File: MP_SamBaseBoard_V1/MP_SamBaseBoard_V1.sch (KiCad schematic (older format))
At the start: 135 parts, among them J1 MOTOR-A_CONN, J10 P1_CONN, J11 I2C_CONN, J12 I2C_CONN, J13 SAM_SWD, J14 WS2812_EXT, J15 PWR_JACK, J16 USB_B_Micro, J17 BATT_CONN, J2 MOTOR-B_CONN, J3 Adafruit_Feather_CONN, J4 DM3D-SF, J5 Conn_01x02, J6 Conn_01x02, J7 SERVO_CONN, J8 P3_CONN, J9 P2_CONN, Q1 DMP3098L, SW1 RESET, SW2 3v3_PWR_SW, SW3 SW1, SW4 SW2, U1 ESP32-WROOM-32, U10 MPU-6050, U11 IRFHM9331PbF, U12 BD5291FVE-GTR, U13 SST25VF016B-50-4C-S2AF, U2 ATSAMD51J19A-A, U3 74LVC1G125, U4 TPS62135, U5 TPS62086, U6 MAX98357AETE, U7 DRV8833RTY, U8 HDC1080, U9 MCP73871-1CC, Y1 Crystal

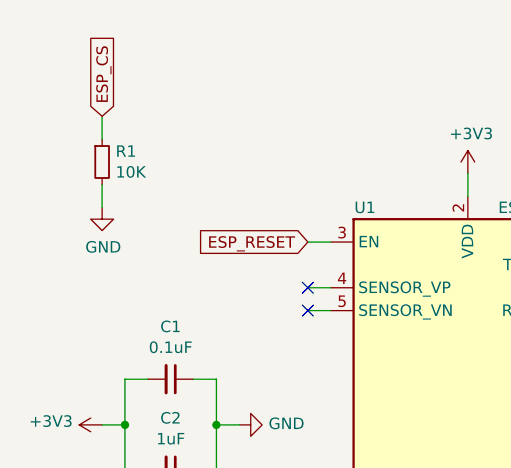
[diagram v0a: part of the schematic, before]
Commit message: Fix pull resistor
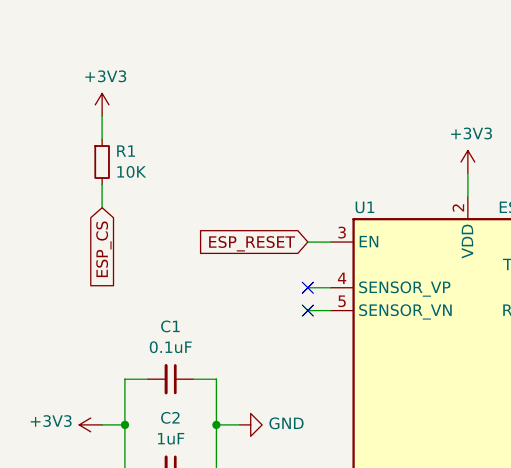
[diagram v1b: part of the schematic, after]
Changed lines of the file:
@@
 Text GLabel 3200 3400 2    50   Input ~ 0
 BLUE_LED
-Text GLabel 900  950  1    50   Input ~ 0
+Text GLabel 900  1350 3    50   Input ~ 0
 ESP_CS
 $Comp
@@
 $EndComp
 $Comp
-L power:GND #PWR0108
-U 1 1 5EBCB51C
-P 900 1350
-F 0 "#PWR0108" H 900 1100 50  0001 C CNN
-F 1 "GND" H 905 1177 50  0000 C CNN
-F 2 "" H 900 1350 50  0001 C CNN
-F 3 "" H 900 1350 50  0001 C CNN
-	1    900  1350
-	1    0    0    -1
-$EndComp
-Wire Wire Line
-	900  1250 900  1350
-Wire Wire Line
-	900  950  900  1050
-$Comp
 L power:GND #PWR0109
 U 1 1 5EBDE57E
@@
 Wire Wire Line
 	2300 10550 2350 10550
+$Comp
+L power:+3V3 #PWR?
+U 1 1 5EDF378B
+P 900 950
+F 0 "#PWR?" H 900 800 50  0001 C CNN
+F 1 "+3V3" H 915 1123 50  0000 C CNN
+F 2 "" H 900 950 50  0001 C CNN
+F 3 "" H 900 950 50  0001 C CNN
+	1    900  950
+	1    0    0    -1
+$EndComp
+Wire Wire Line
+	900  950  900  1050
+Wire Wire Line
+	900  1250 900  1350
 $EndSCHEMATC

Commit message: update
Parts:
- removed C14, C17: 10uF, Capacitor_Tantalum_SMD:CP_EIA-3216-12_Kemet-S, symbol Device:C_Small
- removed D8: PWR_LED, LED_SMD:LED_0603_1608Metric, symbol Device:LED
- removed J4: DM3D-SF, Connector_Card:microSD_HC_Hirose_DM3D-SF, symbol Connector:Micro_SD_Card
- removed L2: 0.47uH, GiraffeTech-Inductor:L_0806_2016Metric, symbol Device:L_Small
- removed R11: 10K, Resistor_SMD:R_0603_1608Metric, symbol Device:R_Small
- removed R2: 1M, Resistor_SMD:R_0603_1608Metric, symbol Device:R_Small
- removed R39: 1K, Resistor_SMD:R_0603_1608Metric, symbol Device:R_Small
- removed U5: TPS62086, GiraffeTech-Texas:Texas_VSON7, symbol InGarage_Regulator_Switching:TPS62086
- added C? (x2): 10uF, symbol Device:C_Small
- added R?: 10K, symbol Device:R_Small
- added U?: LD39200PU33R, Package_DFN_QFN:DFN-6-1EP_3x3mm_P0.95mm_EP1.7x2.6mm, symbol InGarage_Regulator_Linear:LD39200PU33R
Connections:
- wire segments 658 -> 643
- no-connect marks 47 -> 46
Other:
- moved on the sheet: SW2

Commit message: update
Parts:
- removed C28, C29, C44: 0.1uF, Capacitor_SMD:C_0603_1608Metric, symbol Device:C_Small
- removed C30: 2.2nF, Capacitor_SMD:C_0603_1608Metric, symbol Device:C_Small
- removed C31: 1uF, Capacitor_SMD:C_0603_1608Metric, symbol Device:C_Small
- removed C32, C33: 4.7uF, Capacitor_SMD:C_0603_1608Metric, symbol Device:C_Small
- removed D3: LED, LED_SMD:LED_0603_1608Metric, symbol Device:LED
- removed J6: Conn_01x02, GiraffeTech-Connector:DINKLE_EK500V-2P, symbol Connector_Generic:Conn_01x02
- removed R12, R21, R22, R23, R26, R27, R28: 10K, Resistor_SMD:R_0603_1608Metric, symbol Device:R_Small
- removed R20: 1K, Resistor_SMD:R_0603_1608Metric, symbol Device:R_Small
- removed R29: 820K, Resistor_SMD:R_0603_1608Metric, symbol Device:R_Small
- removed U10: MPU-6050, Sensor_Motion:InvenSense_QFN-24_4x4mm_P0.5mm, symbol Sensor_Motion:MPU-6050
- removed U12: BD5291FVE-GTR, Package_TO_SOT_SMD:SOT-353_SC-70-5, symbol pspice:OPAMP
- removed U6: MAX98357AETE, Package_DFN_QFN:TQFN-16-1EP_3x3mm_P0.5mm_EP1.23x1.23mm, symbol InGarage_Audio_Amplifier:MAX98357AETE
- removed U9: MCP73871-1CC, Package_DFN_QFN:QFN-20-1EP_4x4mm_P0.5mm_EP2.5x2.5mm, symbol Battery_Management:MCP73871-1CC
- added C14: 0.1uF, Capacitor_SMD:C_0603_1608Metric, symbol Device:C_Small
- added C17: 10uF, symbol Device:C_Small
- added J4: LOAD_CONN, GiraffeTech-Connector:TerminalBlock_DEGSON_DG300-5-3pol, symbol Connector_Generic:Conn_01x03
- added R11: 780, Resistor_SMD:R_0603_1608Metric, symbol Device:R_Small
- added R2: 10K, symbol Device:R_Small
- added U5: PAM8301, Package_TO_SOT_SMD:SOT-23-6, symbol Amplifier_Audio:PAM8301
- added U6: BQ24075, symbol Battery_Management:BQ24075
- C21: value 0.1uF -> 4.7uF
- C26: value 10uF -> 4.7uF; footprint Capacitor_Tantalum_SMD:CP_EIA-3216-12_Kemet-S -> Capacitor_SMD:C_0603_1608Metric
- D1, D2: footprint LED_SMD:LED_0603_1608Metric -> (none)
- J1, J2: footprint GiraffeTech-Connector:DINKLE_EK500V-2P -> GiraffeTech-Connector:TerminalBlock_DEGSON_DG300-5-2pol
- J5: value Conn_01x02 -> SPEAKER
- L3: footprint GiraffeTech-Inductor:L_1616_2020Metric -> GiraffeTech-Inductor:SPM6530T; Mfg. Part IHLP2020CZER1R0M01 -> SPM6530T-1R0M120
- R13, R17: value 10K -> 1K
- R14: value 10K -> 20K
- R16, R18: value 1K -> 10K
- R19: value 2K -> 1K
- SW2: footprint GiraffeTech-Electromechanical:SW_SPDT_CK-JS102011JCQN -> GiraffeTech-Alps:SSSS811101
- gave numbers to parts that had none: 4
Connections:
- net PROG2 is gone; now on net GND: R14.2
- net REG_SEL is gone; now on net GND: R15.2
- net STAT1 is gone; now on net GND: D2.1 (K)
- net ~PG is gone; now on net GND: D1.1 (K)
- net ~TE is gone; now on net GND: R13.2
- net +3V3: now also C29.1, U9.1 (OUT), U9.2 (SENSE), R2.2, U5.5 (VDD); no longer C21.1
- net +5V: now also C17.1, U6.13 (IN); no longer R13.1, R14.1, R15.1, R16.1, R18.1
- net +BATT: now also U6.2 (BAT), U6.3 (BAT)
- net Adf_A0_DAC0: now also C14.2
- net Adf_A1_DAC1: no longer SW3.1
- net Adf_A3: no longer SW4.1
- net Adf_A5: now also MK1.1 (OUT)
- net CHG_OUT: now also C21.1, R18.1, U6.10 (OUT), U6.11 (OUT)
- net D0_RxD0: now also SW3.1; no longer U1.9 (IO33)
- net D1_TxD0: now also SW4.1
- net GND: now also R16.1, C17.2, J4.3 (Pin_3), R11.2, U5.2 (GND), U6.15 (SYSOFF), U6.17 (PAD), U6.4 (~CE), U6.8 (VSS); no longer R17.2, R19.2
- net VIN: now also J4.1 (Pin_1)
- net at D2.2 (A): now also R19.2; no longer R18.2
- net at D1.2 (A): now also R17.2; no longer R16.2
- net at U11.1 (SOURCE), U11.2 (SOURCE), U11.3 (SOURCE): now also J4.2 (Pin_2)
- net at J5.1 (Pin_1): now also U5.6 (OUT+)
- net at J5.2 (Pin_2): now also U5.1 (OUT-)
- net Adf_D13 renamed ESP_BUSY-D13
- net ESP_BUSY-D13: now also U1.9 (IO33)
- net Adf_D2 renamed ESP_RESET-D2
- net Adf_D3 renamed ESP_IO0-D3
- net Adf_D8 renamed ESP_CS-D8
- net ESP_CS-D8: no longer R1.2
- net PROG1 renamed ~CHG
- net ~CHG: now also U6.9 (~CHG)
- net PROG3 renamed ~PGOOD
- net ~PGOOD: now also U6.7 (~PGOOD)
- new net: C14.1, U5.3 (IN)
- new net: R2.1, U5.4 (~SD)
- new net EN1: R16.2, U6.6 (EN1)
- new net EN2: R18.2, U6.5 (EN2)
- new net ESP_CS: R1.2
- new net ILIM: R11.1, U6.12 (ILIM)
- new net ISET: R13.1, U6.16 (ISET)
- new net TMR: R14.1, U6.14 (TMR)
- new net TS: R15.1, U6.1 (TS)
- no-connect marks 46 -> 39
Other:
- note added: "ANALOG AMPLIFIER"
- note added: "Fast Charge Setting"
- note added: "Input Current Limit"
- note added: "Micro-USB"
- note added: "PUSH BUTTON"
- note added: "SAM PROG CONN"
- note added: "SERVO MOTOR CONN"
- note added: "SPI FLASH MEMORY"
- note added: "WS2812 RGB LED"
- note removed: "I2S AMPLIFIER"
- note removed: "MEMORY"
- moved on the sheet: BZ1, C19, C22, C26, C28, C29, C42, C43, D6, D7, J13, J15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

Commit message: update
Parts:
- removed C11, C18: 10uF, Capacitor_Tantalum_SMD:CP_EIA-3216-12_Kemet-S, symbol Device:C_Small
- removed C17, C28, C29: 10uF, symbol Device:C_Small
- removed C23: 10uF 16V, Capacitor_Tantalum_SMD:CP_EIA-3216-12_Kemet-S, symbol Device:C_Small
- removed U8: HDC1080, Package_SON:Texas_PWSON-N6, symbol Sensor_Humidity:HDC1080
- added C11, C17, C18, C23, C28, C29: 10uF, Capacitor_Tantalum_SMD:CP_EIA-3216-12_Kemet-S, symbol Device:CP_Small
- added C30, C31: 0.1uF, Capacitor_SMD:C_0603_1608Metric, symbol Device:C_Small
- added H1, H2, H3, H4: 3.5mm, MountingHole:MountingHole_3.5mm, symbol Mechanical:MountingHole
- added Q2: ALS-PT19-315C/L177/TR8, Diode_SMD:D_0603_1608Metric, symbol Device:Q_Photo_NPN_EC
- added R20, R21, R22: 10K, Resistor_SMD:R_0603_1608Metric, symbol Device:R_Small
- added U10: KXTJ3-1057, Package_LGA:LGA-12_2x2mm_P0.5mm, symbol InGarage_Sensor_Motion:KXTJ3-1057
- added U8: Sensirion_SHT3x, GiraffeTech-Sensiroin:Sensirion_SHT3x, symbol InGarage_Sensor_Environment:Sensirion_SHT3x
- D1, D2: footprint (none) -> LED_SMD:LED_0603_1608Metric
- J1: value MOTOR-A_CONN -> MA_CONN; footprint GiraffeTech-Connector:TerminalBlock_DEGSON_DG300-5-2pol -> GiraffeTech-Connector:TerminalBlock_Dinkle_ED350V_1x02_P3.50mm_Horizontal
- J2: value MOTOR-B_CONN -> MB_CONN
- R12, R2: footprint (none) -> Resistor_SMD:R_0603_1608Metric
- SW1, SW3, SW4: footprint Button_Switch_SMD:SW_SPST_B3S-1000 -> GiraffeTech-Electromechanical:SW_Push_TS-1145A-B-A
- U6: footprint (none) -> Package_DFN_QFN:VQFN-16-1EP_3x3mm_P0.5mm_EP1.6x1.6mm_ThermalVias
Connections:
- net +3V3: now also C28.1, C30.1, C31.1, Q2.2 (C), R21.1, R22.1, U10.10 (VDD), U10.11 (IO_VDD), U10.3 (IO_VDD), U10.7 (VDD), U8.5 (VDD)
- net +5V: now also C17.1, C29.1
- net Adf_A0_DAC0: no longer J10.4 (Pin_4)
- net Adf_A1_DAC1: now also J10.4 (Pin_4); no longer J10.3 (Pin_3)
- net Adf_A3: now also J8.4 (Pin_4); no longer J9.3 (Pin_3)
- net Adf_A4: now also Q2.1 (E), R20.1; no longer J8.4 (Pin_4)
- net Adf_D4: no longer J8.3 (Pin_3)
- net CHG_OUT: now also C23.1
- net D0_RxD0: now also J10.3 (Pin_3), U1.35 (TXD0/IO1); no longer U1.34 (RXD0/IO3)
- net D1_TxD0: now also J9.3 (Pin_3), U1.34 (RXD0/IO3); no longer U1.35 (TXD0/IO1)
- net GND: now also C11.2, C17.2, C18.2, C23.2, C28.2, C29.2, C30.2, C31.2, R20.2, U10.1 (ADDR), U10.4 (RES), U10.6 (GND), U10.8 (GND), U10.9 (GND), U8.2 (ADDR), U8.7 (R), U8.8 (VSS), U8.9 (PAD)
- net I2C_SCL: now also R21.2, U10.12 (SCL), U8.4 (SCL)
- net I2C_SDA: now also R22.2, U10.2 (SDA), U8.1 (SDA)
- net VIN: now also C11.1, C18.1
- no-connect marks 39 -> 43
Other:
- note added: "LIGHT SENSOR"
- moved on the sheet: C22, J7

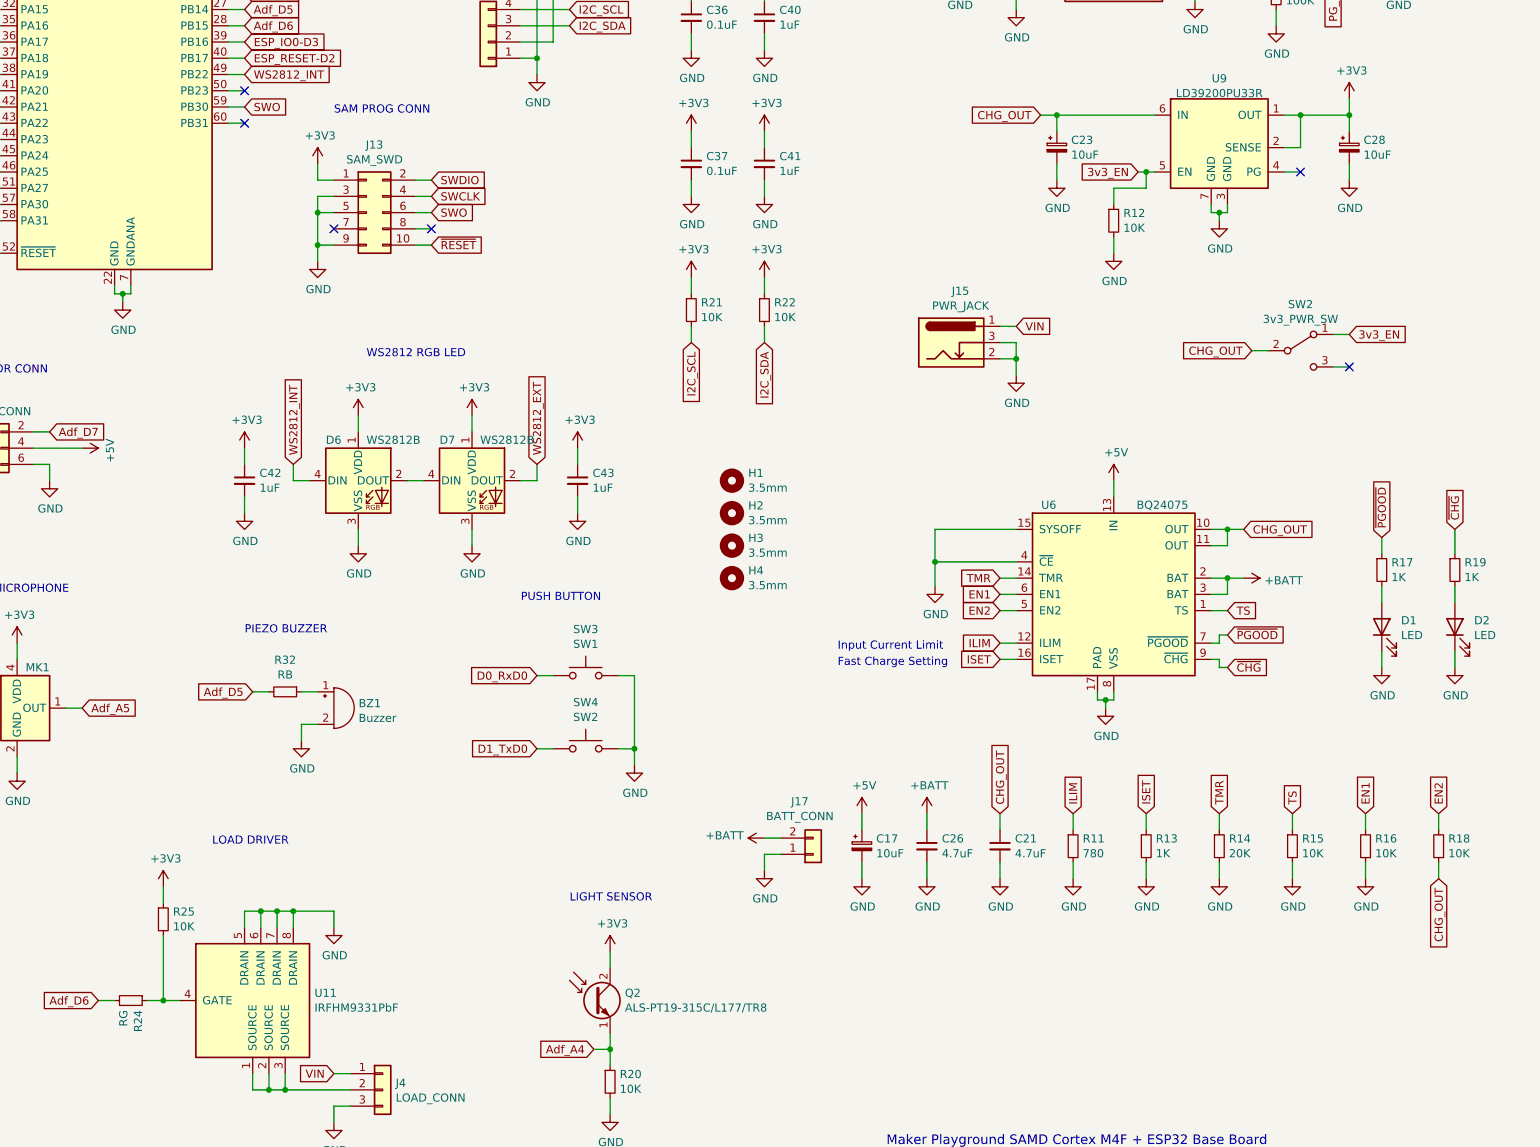
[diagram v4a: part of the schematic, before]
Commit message: Add missing components, edit foorprint
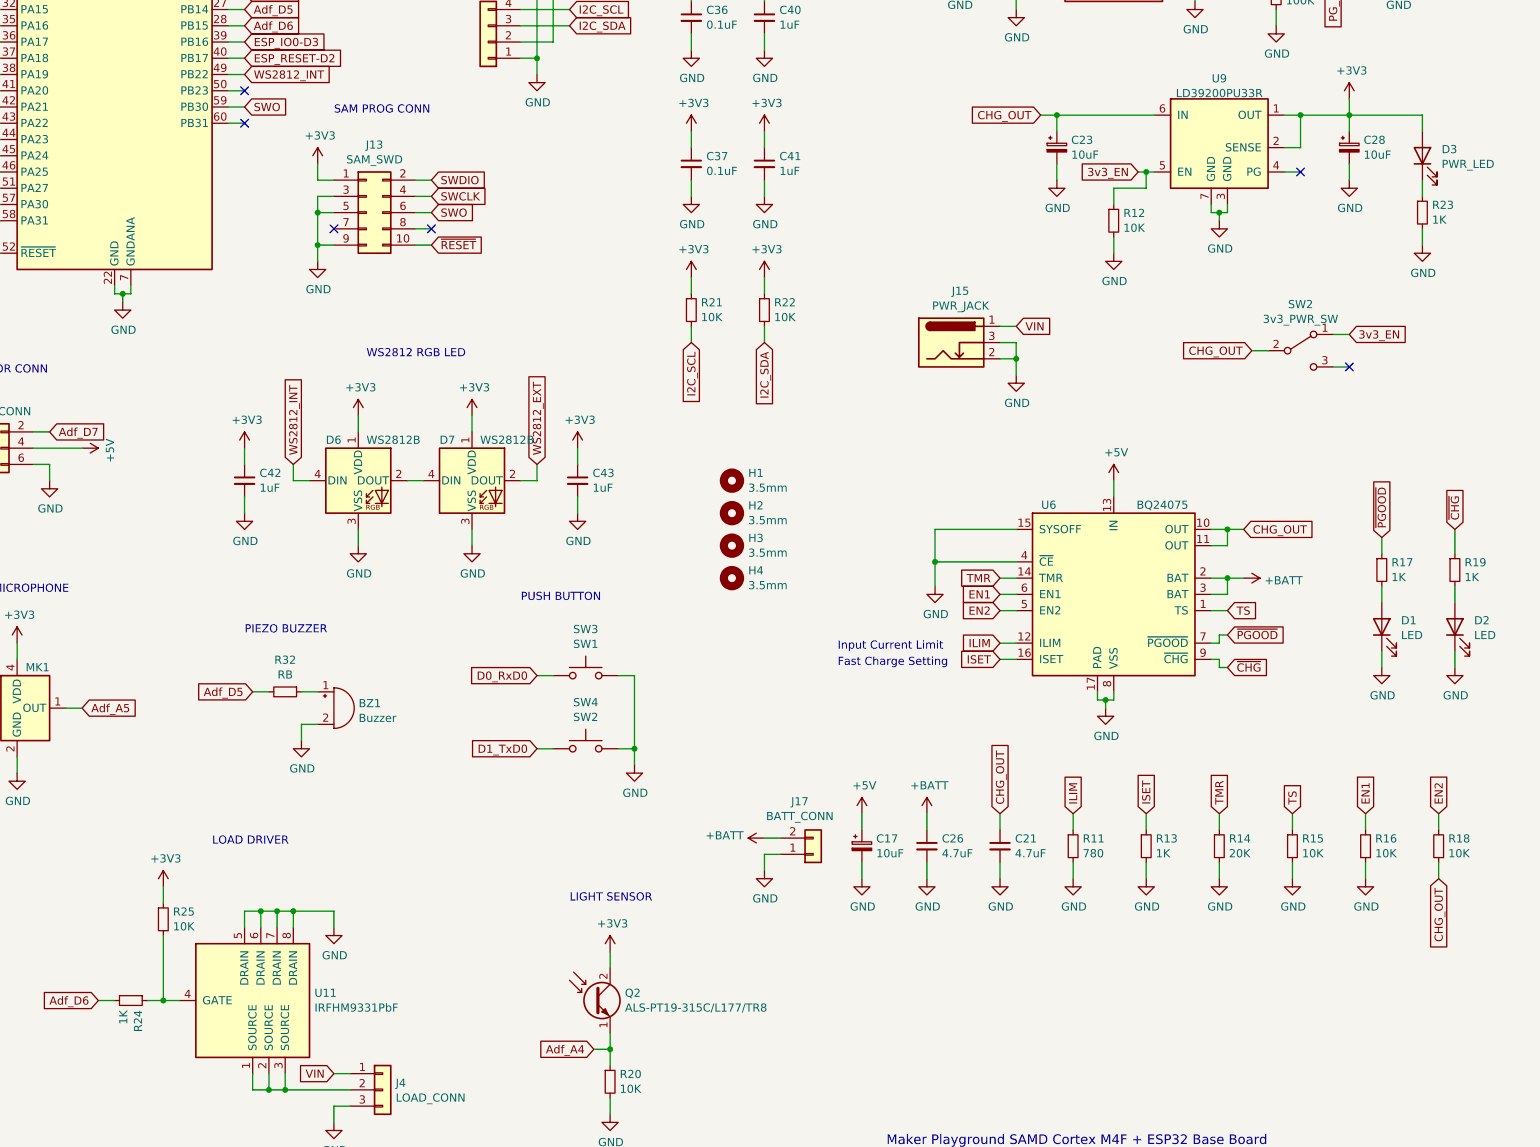
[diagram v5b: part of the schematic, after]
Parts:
- added D3: PWR_LED, LED_SMD:LED_0603_1608Metric, symbol Device:LED
- added R23: 1K, Resistor_SMD:R_0603_1608Metric, symbol Device:R_Small
- J2: footprint GiraffeTech-Connector:TerminalBlock_DEGSON_DG300-5-2pol -> GiraffeTech-Connector:TerminalBlock_Dinkle_ED350V_1x02_P3.50mm_Horizontal
- R24: value RG -> 1K
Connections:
- net +3V3: now also D3.2 (A)
- net GND: now also R23.2
- new net: D3.1 (K), R23.1
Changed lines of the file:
@@
 F 0 "J2" H 3480 8642 50  0000 L CNN
 F 1 "MB_CONN" H 3480 8551 50  0000 L CNN
-F 2 "GiraffeTech-Connector:TerminalBlock_DEGSON_DG300-5-2pol" H 3400 8650 50  0001 C CNN
+F 2 "GiraffeTech-Connector:TerminalBlock_Dinkle_ED350V_1x02_P3.50mm_Horizontal" H 3400 8650 50  0001 C CNN
 F 3 "~" H 3400 8650 50  0001 C CNN
 	1    3400 8650
@@
 P 7550 10050
 F 0 "R24" H 7609 10096 50  0000 L CNN
-F 1 "RG" H 7609 10005 50  0000 L CNN
+F 1 "1K" H 7609 10005 50  0000 L CNN
 F 2 "Resistor_SMD:R_0603_1608Metric" H 7550 10050 50  0001 C CNN
 F 3 "~" H 7550 10050 50  0001 C CNN
@@
 Adf_A3
 NoConn ~ 10250 1250
+$Comp
+L Device:LED D3
+U 1 1 5EE5D35E
+P 15500 4850
+F 0 "D3" V 15539 4732 50  0000 R CNN
+F 1 "PWR_LED" V 15448 4732 50  0000 R CNN
+F 2 "LED_SMD:LED_0603_1608Metric" H 15500 4850 50  0001 C CNN
+F 3 "~" H 15500 4850 50  0001 C CNN
+	1    15500 4850
+	0    -1   -1   0
+$EndComp
+$Comp
+L power:GND #PWR0197
+U 1 1 5EE5DFBB
+P 15500 5400
+F 0 "#PWR0197" H 15500 5150 50  0001 C CNN
+F 1 "GND" H 15505 5227 50  0000 C CNN
+F 2 "" H 15500 5400 50  0001 C CNN
+F 3 "" H 15500 5400 50  0001 C CNN
+	1    15500 5400
+	1    0    0    -1
+$EndComp
+$Comp
+L Device:R_Small R23
+U 1 1 5EE5E86B
+P 15500 5200
+F 0 "R23" H 15559 5246 50  0000 L CNN
+F 1 "1K" H 15559 5155 50  0000 L CNN
+F 2 "Resistor_SMD:R_0603_1608Metric" H 15500 5200 50  0001 C CNN
+F 3 "~" H 15500 5200 50  0001 C CNN
+	1    15500 5200
+	1    0    0    -1
+$EndComp
+Wire Wire Line
+	15500 5000 15500 5100
+Wire Wire Line
+	15500 5300 15500 5400
+Wire Wire Line
+	15050 4600 15500 4600
+Wire Wire Line
+	15500 4600 15500 4700
 $EndSCHEMATC
